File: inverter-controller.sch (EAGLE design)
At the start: 140 parts, among them IC1 STM32F334C8T6, IC10 ISO3082, IC2 SY7152ABC, IC3 LMV358MMX, IC4 LMV358MMX, J1 621006245821, J2 61300211121, Q17 1039-2335","DC-DC Converter 5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, X1 0289-9066**15EDGVC-3.81-02P-14, X2 0289-9066**15EDGVC-3.81-02P-14, X3 0289-9068**15EDGVC-3.81-03P-14, X6 1365-16, Y1 NX2016SA-32M

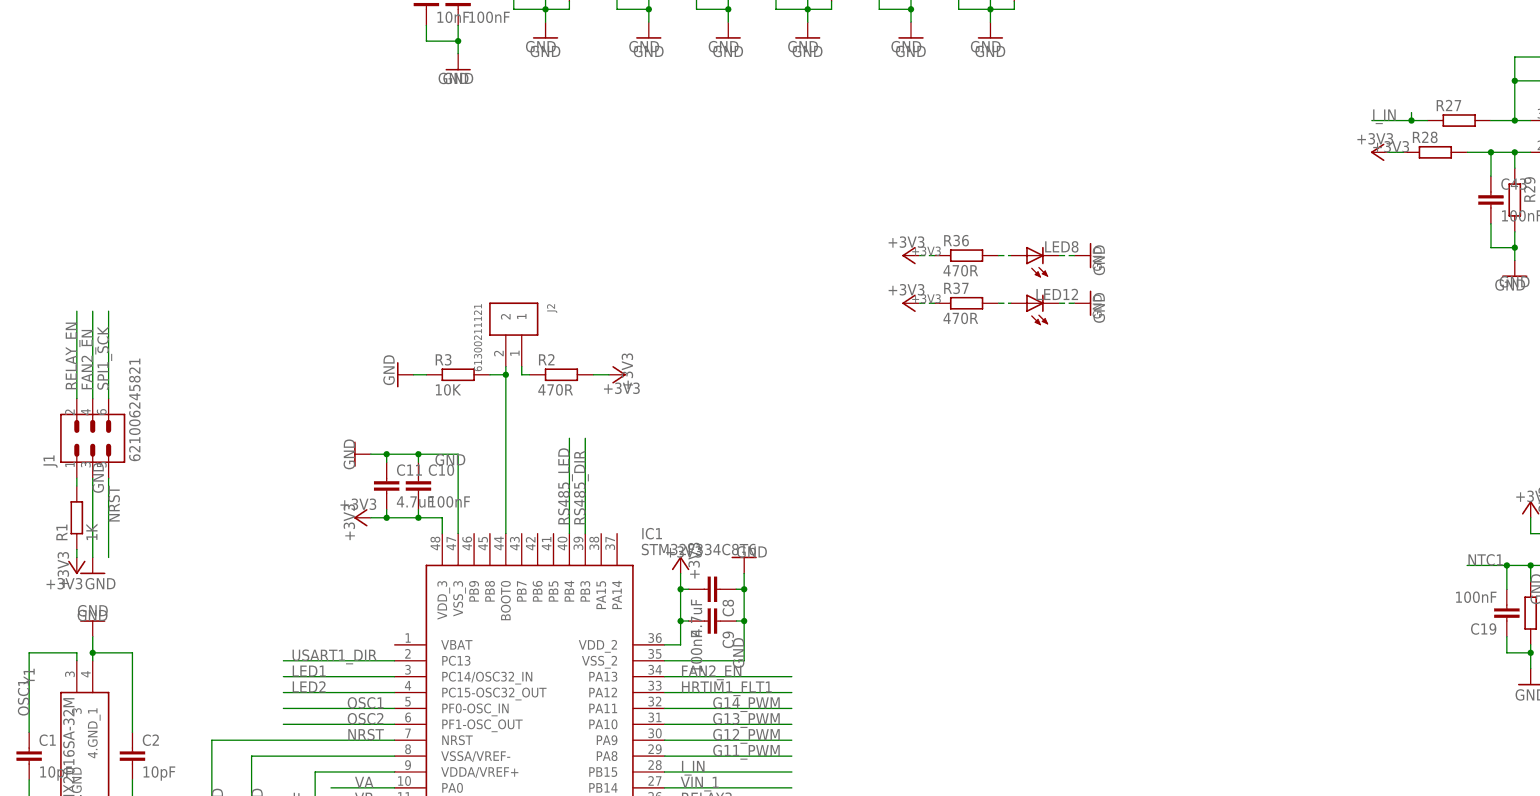
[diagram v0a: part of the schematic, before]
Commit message: Programlama soketi baglantilari duzeltildi.
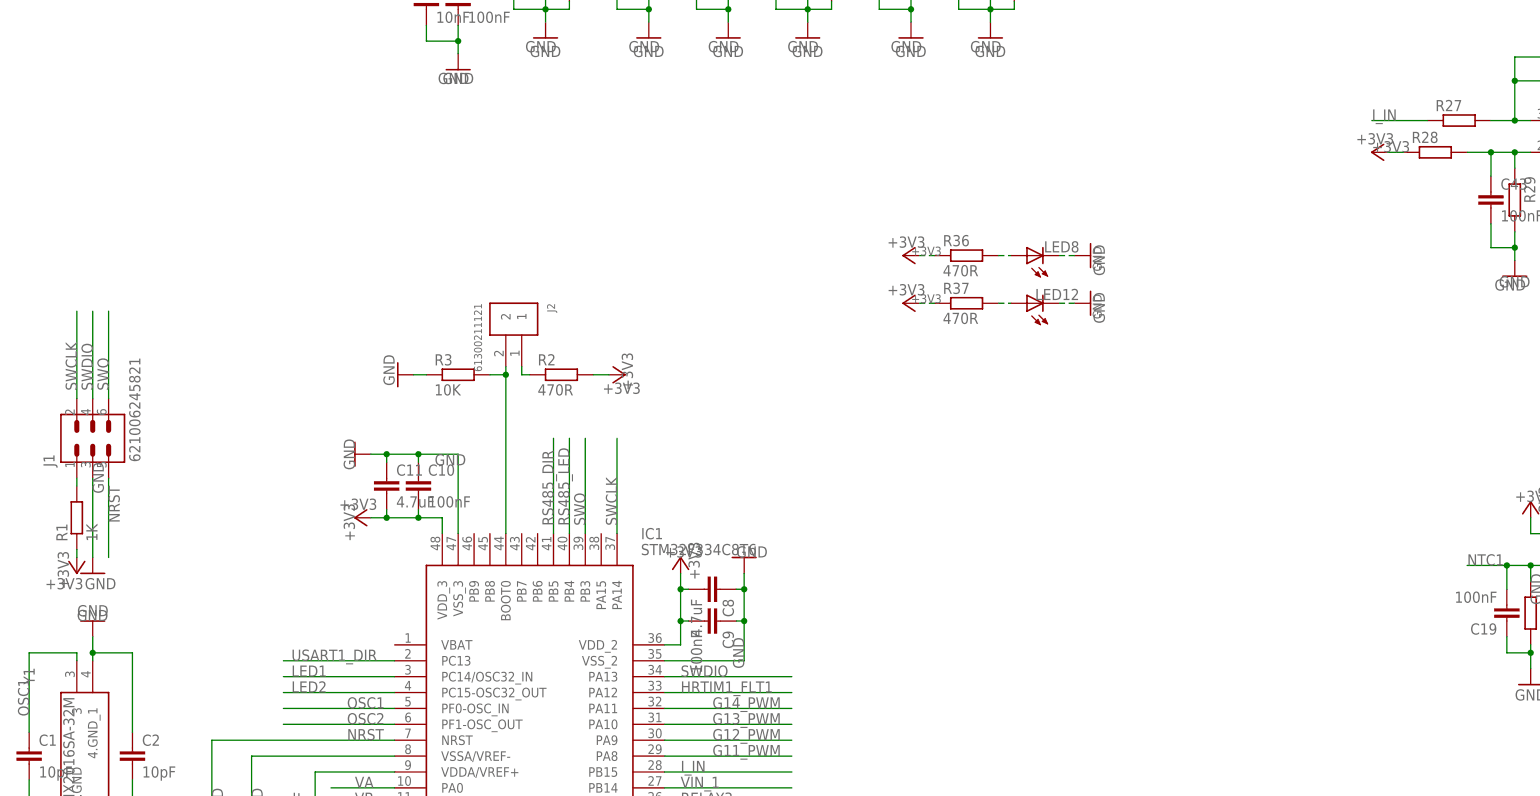
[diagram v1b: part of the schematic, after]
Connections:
- net FAN2_EN renamed SWDIO
- removed net RELAY_EN: J1.2
- removed net SPI1_SCK: J1.6
- new net SWCLK: IC1.PA14, J1.2
- new net SWO: IC1.PB3, J1.6
- net RS485_DIR: now also IC1.PB5; no longer IC1.PB3
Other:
- note removed: "/SWCLK"
- note removed: "/SWDIO"
- note removed: "/SWO"
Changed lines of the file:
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@@
 <text x="5.08" y="149.86" size="5.08" layer="125">uController</text>
 <text x="218.44" y="110.49" size="5.08" layer="125">Temperature Sensors</text>
-<text x="19.05" y="134.62" size="1.9304" layer="125" rot="R90">/SWDIO</text>
-<text x="21.59" y="134.62" size="1.9304" layer="125" rot="R90">/SWO</text>
-<text x="16.51" y="134.62" size="1.4224" layer="125" rot="R90">/SWCLK</text>
 <text x="133.35" y="71.12" size="1.778" layer="125">CHB2</text>
 <text x="133.35" y="68.58" size="1.778" layer="125">CHB1</text>
@@
 </segment>
 </net>
-<net name="SPI1_SCK" class="0">
-<segment>
-<pinref part="J1" gate="G$1" pin="6"/>
-<wire x1="21.59" y1="120.65" x2="21.59" y2="134.62" width="0.1524" layer="91"/>
-<label x="21.59" y="121.92" size="1.778" layer="95" rot="R90"/>
-</segment>
-</net>
 <net name="NRST" class="0">
 <segment>
@@
 <segment>
 <label x="223.52" y="165.1" size="1.778" layer="95"/>
-<wire x1="229.87" y1="165.1" x2="223.52" y2="165.1" width="0.1524" layer="91"/>
-<wire x1="229.87" y1="165.1" x2="229.87" y2="166.37" width="0.1524" layer="91"/>
+<wire x1="232.41" y1="165.1" x2="223.52" y2="165.1" width="0.1524" layer="91"/>
 <pinref part="R27" gate="G$1" pin="1"/>
-<wire x1="229.87" y1="165.1" x2="232.41" y2="165.1" width="0.1524" layer="91"/>
-<junction x="229.87" y="165.1"/>
 </segment>
 <segment>
@@
 </segment>
 </net>
-<net name="FAN2_EN" class="0">
-<segment>
-<pinref part="IC1" gate="G$1" pin="PA13"/>
-<wire x1="110.49" y1="76.2" x2="130.81" y2="76.2" width="0.1524" layer="91"/>
-<label x="113.03" y="76.2" size="1.778" layer="95"/>
-</segment>
-<segment>
-<pinref part="J1" gate="G$1" pin="4"/>
-<wire x1="19.05" y1="120.65" x2="19.05" y2="134.62" width="0.1524" layer="91"/>
-<label x="19.05" y="121.92" size="1.778" layer="95" rot="R90"/>
-</segment>
-</net>
-<net name="RELAY_EN" class="0">
-<segment>
-<pinref part="J1" gate="G$1" pin="2"/>
-<wire x1="16.51" y1="120.65" x2="16.51" y2="134.62" width="0.1524" layer="91"/>
-<label x="16.51" y="121.92" size="1.778" layer="95" rot="R90"/>
-</segment>
-</net>
 <net name="N$35" class="0">
 <segment>
@@
 </segment>
 <segment>
-<pinref part="IC1" gate="G$1" pin="PB3"/>
-<wire x1="97.79" y1="99.06" x2="97.79" y2="114.3" width="0.1524" layer="91"/>
-<label x="97.79" y="100.33" size="1.778" layer="95" rot="R90"/>
+<pinref part="IC1" gate="G$1" pin="PB5"/>
+<wire x1="92.71" y1="99.06" x2="92.71" y2="114.3" width="0.1524" layer="91"/>
+<label x="92.71" y="100.33" size="1.778" layer="95" rot="R90"/>
 </segment>
 </net>
@@
 </segment>
 </net>
+<net name="SWO" class="0">
+<segment>
+<pinref part="IC1" gate="G$1" pin="PB3"/>
+<wire x1="97.79" y1="99.06" x2="97.79" y2="114.3" width="0.1524" layer="91"/>
+<label x="97.79" y="100.33" size="1.778" layer="95" rot="R90"/>
+</segment>
+<segment>
+<pinref part="J1" gate="G$1" pin="6"/>
+<wire x1="21.59" y1="120.65" x2="21.59" y2="134.62" width="0.1524" layer="91"/>
+<label x="21.59" y="121.92" size="1.778" layer="95" rot="R90"/>
+</segment>
+</net>
+<net name="SWDIO" class="0">
+<segment>
+<pinref part="IC1" gate="G$1" pin="PA13"/>
+<wire x1="110.49" y1="76.2" x2="130.81" y2="76.2" width="0.1524" layer="91"/>
+<label x="113.03" y="76.2" size="1.778" layer="95"/>
+</segment>
+<segment>
+<pinref part="J1" gate="G$1" pin="4"/>
+<wire x1="19.05" y1="120.65" x2="19.05" y2="134.62" width="0.1524" layer="91"/>
+<label x="19.05" y="121.92" size="1.778" layer="95" rot="R90"/>
+</segment>
+</net>
+<net name="SWCLK" class="0">
+<segment>
+<pinref part="IC1" gate="G$1" pin="PA14"/>
+<wire x1="102.87" y1="99.06" x2="102.87" y2="114.3" width="0.1524" layer="91"/>
+<label x="102.87" y="100.33" size="1.778" layer="95" rot="R90"/>
+</segment>
+<segment>
+<pinref part="J1" gate="G$1" pin="2"/>
+<wire x1="16.51" y1="120.65" x2="16.51" y2="134.62" width="0.1524" layer="91"/>
+<label x="16.51" y="121.92" size="1.778" layer="95" rot="R90"/>
+</segment>
+</net>

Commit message: RS485 DC-DC paketi degistirildi.
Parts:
- removed Q17: 1039-2335","DC-DC Converter 5V to 5V 1W RFMM-0505S, enko:RFMM-0505S
- added DC7: RI-0512S/P_DC_DC_5V_12V, my_parts1:RI-0512S/P_DC_DC_5V_12V
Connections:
- removed net RELAY3: IC1.PB13
- removed net USART1_DIR: IC1.PC13
- net GND: now also DC7.1.VIN-; no longer Q17.VIN-
- net N$80: now also DC7.2.VIN+; no longer Q17.VIN+
- net RS485_ISO_5V: now also DC7.4.VOUT+; no longer Q17.VOUT+
- net RS485_ISO_GND: now also DC7.3.VOUT-; no longer Q17.VOUT-
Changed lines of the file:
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@@
 <part name="X3" library="con-phoenix-381_l" deviceset="MCV3" device="" value="0289-9068**15EDGVC-3.81-03P-14"/>
 <part name="+3V8" library="supply1" deviceset="+3V3" device=""/>
-<part name="Q17" library="enko" deviceset="RFMM-0505S" device="" value="1039-2335&quot;,&quot;DC-DC Converter 5V to 5V 1W RFMM-0505S"/>
 <part name="C51" library="rcl" deviceset="C-EU" device="C0805" value="1019-3168&quot;,&quot;CAP 0805 CER 2.2uF 16V %10 X7R (AbC)"/>
 <part name="C52" library="rcl" deviceset="C-EU" device="050-055X075" value="0019-3020&quot;,&quot;CAP TH CER 470pF 3kV Y5P %10 85C F=7.5 D=8.5"/>
@@
 <part name="+3V16" library="supply1" deviceset="+3V3" device=""/>
 <part name="+3V17" library="supply1" deviceset="+3V3" device=""/>
+<part name="DC7" library="my_parts1" deviceset="RI-0512S/P_DC_DC_5V_12V" device=""/>
 </parts>
 <sheets>
@@
 <attribute name="VALUE" x="364.49" y="231.14" size="1.778" layer="96" rot="R90"/>
 </instance>
-<instance part="Q17" gate="G$1" x="414.02" y="163.83" smashed="yes">
-<attribute name="NAME" x="403.86" y="172.72" size="1.778" layer="95"/>
-<attribute name="VALUE" x="403.86" y="158.75" size="1.778" layer="96"/>
-</instance>
 <instance part="C51" gate="G$1" x="381" y="165.1" smashed="yes" rot="MR0">
 <attribute name="NAME" x="376.301" y="166.116" size="1.778" layer="95" rot="R270"/>
@@
 <instance part="+3V17" gate="G$1" x="381" y="173.99" smashed="yes">
 <attribute name="VALUE" x="378.46" y="168.91" size="1.778" layer="96" rot="R90"/>
+</instance>
+<instance part="DC7" gate="G$1" x="414.02" y="166.37" smashed="yes">
+<attribute name="NAME" x="403.86" y="172.72" size="1.778" layer="95"/>
+<attribute name="VALUE" x="403.86" y="158.75" size="1.778" layer="96"/>
 </instance>
 </instances>
@@
 <wire x1="82.55" y1="124.46" x2="85.09" y2="124.46" width="0.1524" layer="91"/>
 <junction x="85.09" y="124.46"/>
-</segment>
-</net>
-<net name="USART1_DIR" class="0">
-<segment>
-<pinref part="IC1" gate="G$1" pin="PC13"/>
-<wire x1="67.31" y1="78.74" x2="49.53" y2="78.74" width="0.1524" layer="91"/>
-<label x="50.8" y="78.74" size="1.778" layer="95"/>
 </segment>
 </net>
@@
 <wire x1="381" y1="158.75" x2="398.78" y2="158.75" width="0.1524" layer="91"/>
 <wire x1="398.78" y1="158.75" x2="398.78" y2="163.83" width="0.1524" layer="91"/>
-<pinref part="Q17" gate="G$1" pin="VIN-"/>
 <wire x1="398.78" y1="163.83" x2="401.32" y2="163.83" width="0.1524" layer="91"/>
 <label x="378.46" y="149.86" size="1.778" layer="95"/>
@@
 <pinref part="GND32" gate="1" pin="GND"/>
 <wire x1="381" y1="154.94" x2="381" y2="158.75" width="0.1524" layer="91"/>
+<pinref part="DC7" gate="G$1" pin="1.VIN-"/>
 </segment>
 </net>
@@
 </segment>
 </net>
-<net name="RELAY3" class="0">
-<segment>
-<pinref part="IC1" gate="G$1" pin="PB13"/>
-<wire x1="110.49" y1="55.88" x2="130.81" y2="55.88" width="0.1524" layer="91"/>
-<label x="113.03" y="55.88" size="1.778" layer="95"/>
-</segment>
-</net>
 <net name="LED2" class="0">
 <segment>
@@
 <net name="N$80" class="0">
 <segment>
-<pinref part="Q17" gate="G$1" pin="VIN+"/>
 <wire x1="394.97" y1="168.91" x2="398.78" y2="168.91" width="0.1524" layer="91"/>
 <pinref part="C52" gate="G$1" pin="1"/>
@@
 <junction x="398.78" y="168.91"/>
 <pinref part="L1" gate="G$1" pin="2"/>
+<pinref part="DC7" gate="G$1" pin="2.VIN+"/>
 </segment>
 </net>
 <net name="RS485_ISO_5V" class="0">
 <segment>
-<pinref part="Q17" gate="G$1" pin="VOUT+"/>
 <pinref part="SUPPLY5" gate="G$1" pin="+5V/4"/>
 <wire x1="426.72" y1="168.91" x2="431.8" y2="168.91" width="0.1524" layer="91"/>
@@
 <wire x1="431.8" y1="176.53" x2="431.8" y2="168.91" width="0.1524" layer="91"/>
 <label x="439.42" y="177.8" size="1.778" layer="95"/>
+<pinref part="DC7" gate="G$1" pin="4.VOUT+"/>
 </segment>
 <segment>
@@
 <net name="RS485_ISO_GND" class="0">
 <segment>
-<pinref part="Q17" gate="G$1" pin="VOUT-"/>
 <wire x1="426.72" y1="163.83" x2="427.99" y2="163.83" width="0.1524" layer="91"/>
 <wire x1="427.99" y1="163.83" x2="427.99" y2="158.75" width="0.1524" layer="91"/>
@@
 <junction x="431.8" y="158.75"/>
 <label x="434.34" y="158.75" size="1.778" layer="95"/>
-</segment>
-<segment>
+<pinref part="DC7" gate="G$1" pin="3.VOUT-"/>
+</segment>
+<segment>
